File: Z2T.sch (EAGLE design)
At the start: 11 parts, among them J1 M02X7-SOCKET, J2 M02X6-SOCKET

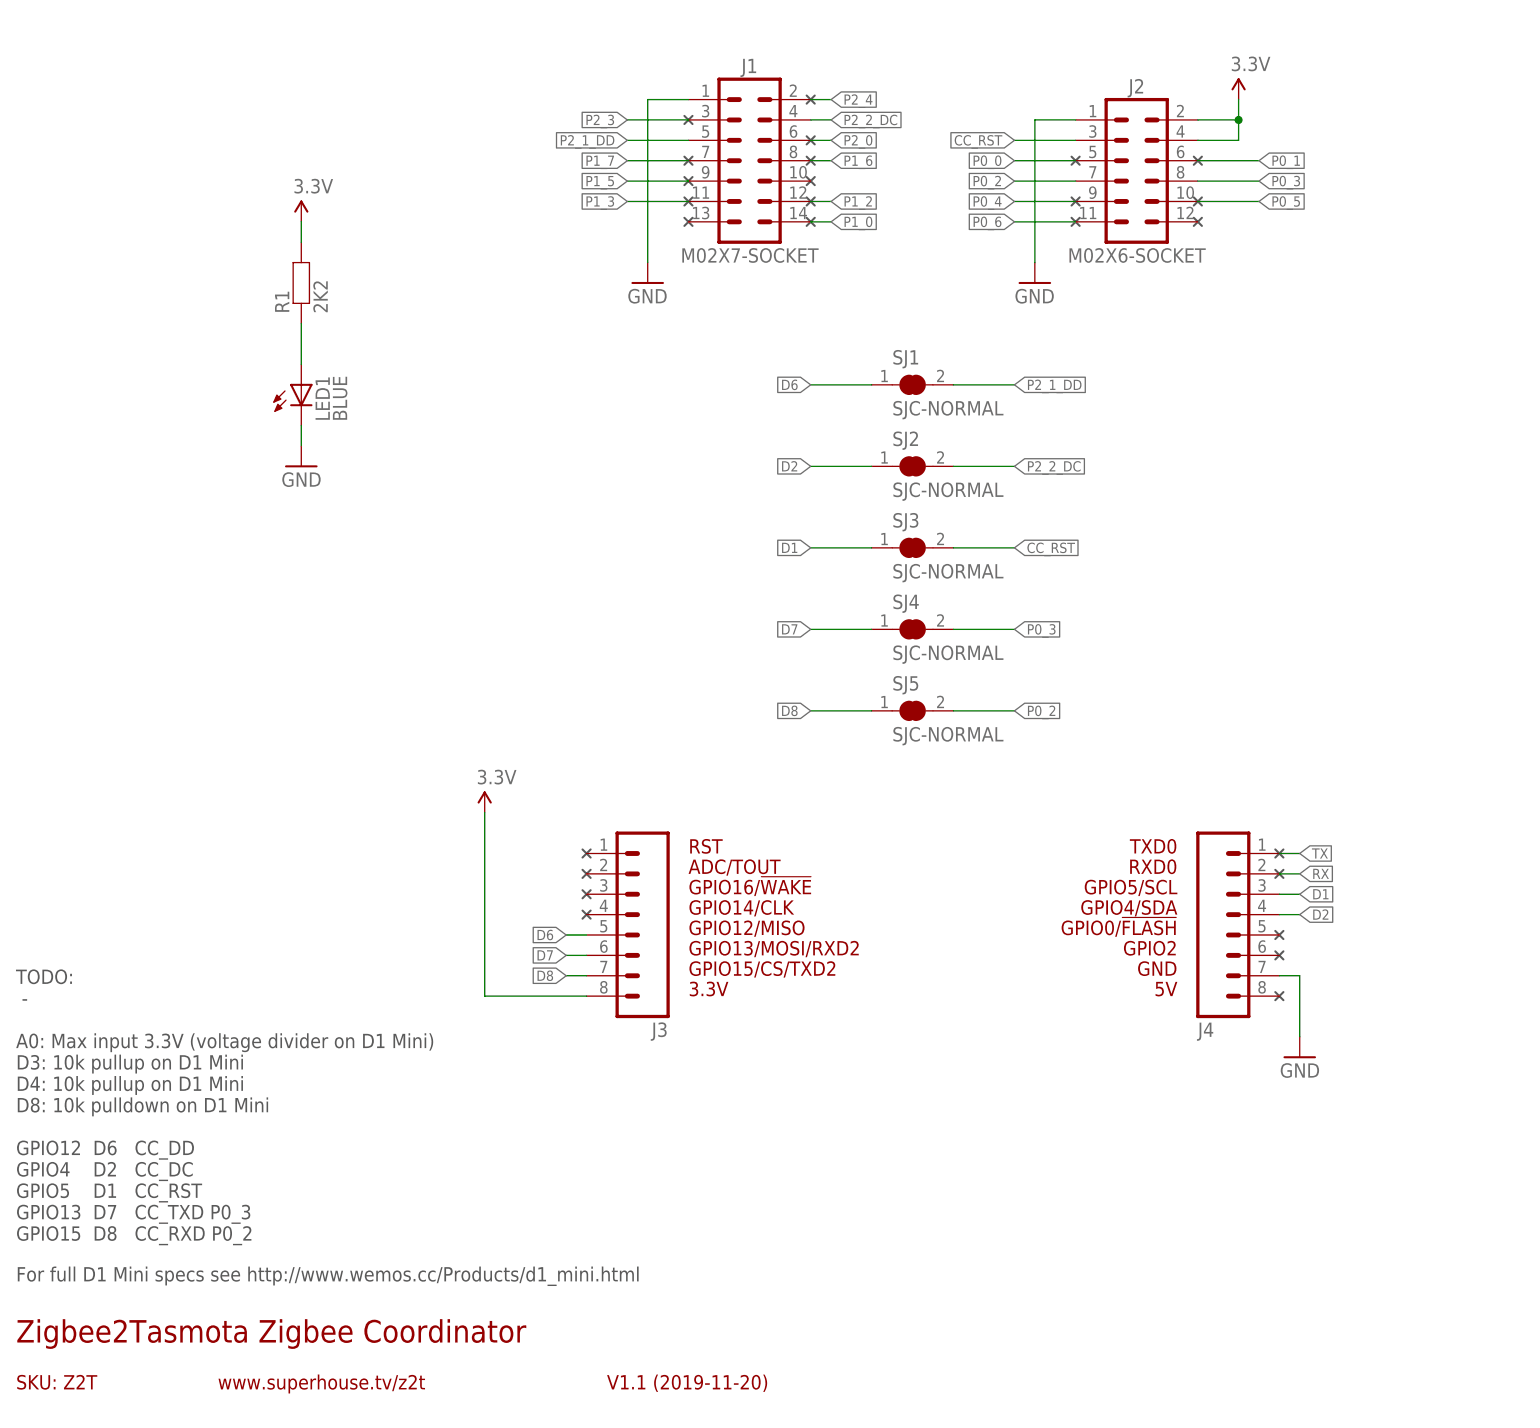
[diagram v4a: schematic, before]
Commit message: Schematic clarification, silkscreen tweaks
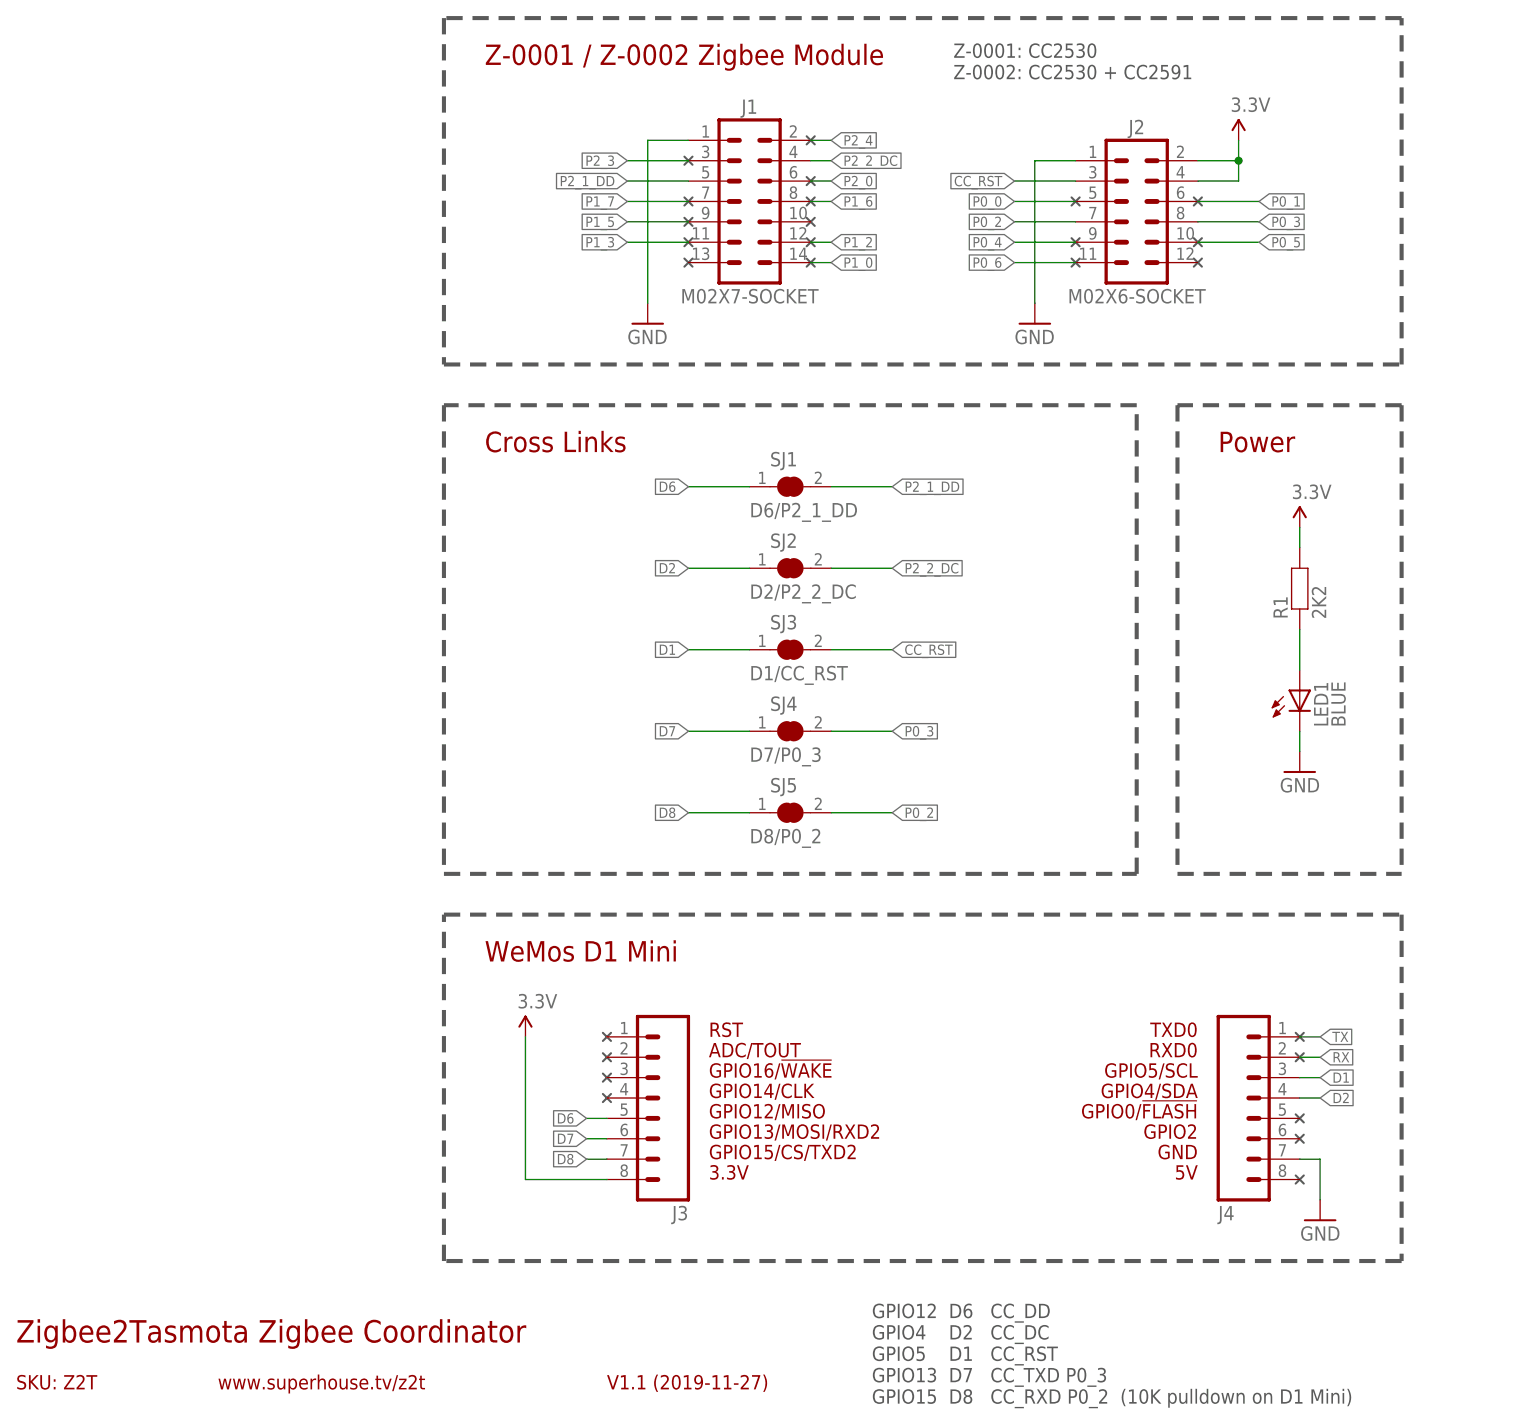
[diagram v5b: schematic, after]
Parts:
- SJ1: value SJC-NORMAL -> D6/P2_1_DD
- SJ2: value SJC-NORMAL -> D2/P2_2_DC
- SJ3: value SJC-NORMAL -> D1/CC_RST
- SJ4: value SJC-NORMAL -> D7/P0_3
- SJ5: value SJC-NORMAL -> D8/P0_2
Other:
- note added: "Cross Links"
- note added: "GPIO12 D6 CC_DD GPIO4 D2 CC_DC GPIO5 D1 CC_RST GPIO13 D7 CC_TXD P0_3 GPIO15 D8 CC_RXD P0_2 (10K pulldown on D1 Mini)"
- note added: "Power"
- note added: "V1.1 (2019-11-27)"
- note added: "WeMos D1 Mini"
- note added: "Z-0001 / Z-0002 Zigbee Module"
- note added: "Z-0001: CC2530 Z-0002: CC2530 + CC2591"
- note removed: "For full D1 Mini specs see http://www.wemos.cc/Products/d1_mini.html"
- note removed: "TODO: - A0: Max input 3.3V (voltage divider on D1 Mini) D3: 10k pullup on D1 Mini D4: 10k pullup on D1 Mini D8: 10k pulldown on D1 Mini GPIO12 D6 CC_DD GPIO4 D2 CC_DC GPIO5 D1 CC_RST GPIO13 D7 CC_TXD P0_3 GPIO15 D8 CC_RXD P0_2"
- note removed: "V1.1 (2019-11-20)"
- moved on the sheet: J1, J2, J3, J4, LED1, R1, SJ1, SJ2, SJ3, SJ4, SJ5
